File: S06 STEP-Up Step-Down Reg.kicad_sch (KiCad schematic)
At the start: 54 parts, among them Q16 IAUCN04S7L019, Q17 IAUCN04S7L028, Q18 CSD17304Q3, Q19 IAUCN04S7L019, U5 LM51772RHAR

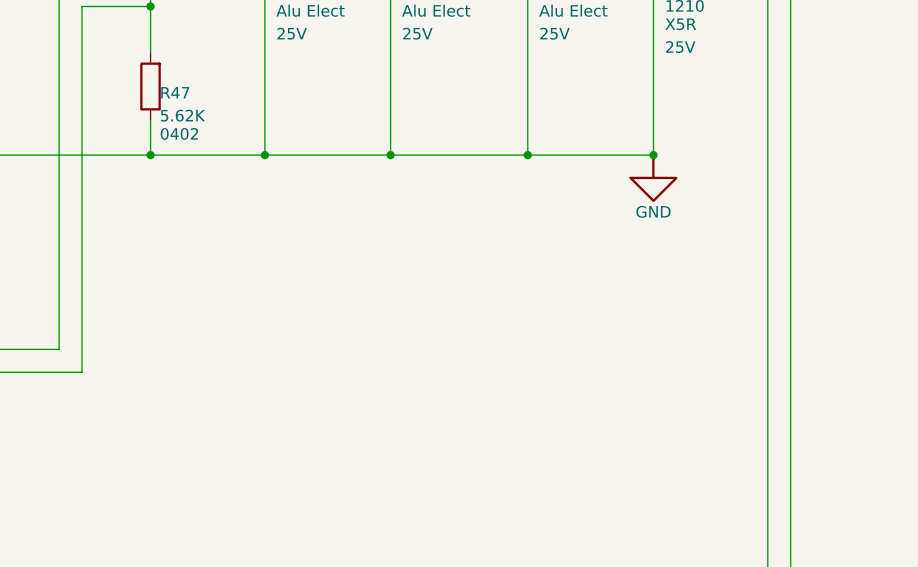
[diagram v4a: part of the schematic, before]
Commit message: Retune load-switch OVLO and PG dividers; add design constraint notes
- R90-R92 1M -> 1.07M: OVLO trips at 14.0 V (13.40-14.69 V) and recovers
  below 12.75 V (at least 12.23 V), so a tripped switch always comes back
  on the 12.03 V rail. R101 (Q23 gate divider) -> 1.07M to share the line.
- PGTH dividers R59/R61/R76 1M -> 100K and R60/R62/R77 130K -> 13K: same
  10.43 V threshold, but the +-1 uA pin leakage now moves it 0.1 V, not
  1 V; worst-case rising 10.93 V instead of 11.84 V.
- Schematic notes for the W16 constraints: J2 contacts (S01), R16 latching
  breaker and ED29/QE29 trip currents (S03), R19 vs L1 saturation (S04),
  R22 presence pull-up (S05), R42 and the U5 MODE/ILIMCOMP/VCC2 pins (S06),
  and the OVLO/PG divider settings (S07).
- README: OVLO and PG divider figures, and the EN_CONST_TDEAD default for
  the I2C build.

Co-Authored-By: Claude Opus 5.5 <noreply@anthropic.com>
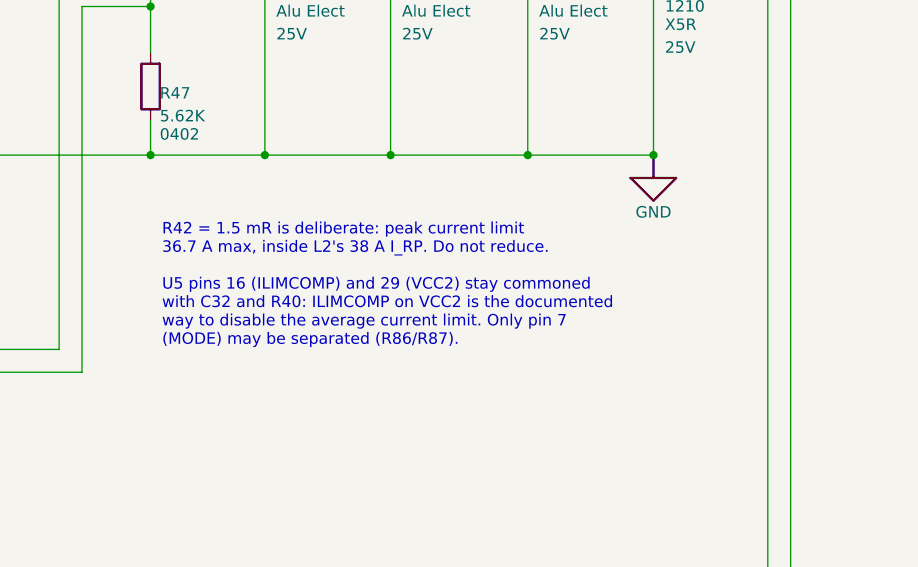
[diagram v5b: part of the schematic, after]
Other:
- note added: "R42 = 1.5 mR is deliberate: peak current limit 36.7 A max, inside L2's 38 A I_RP. Do not reduce. U5 pins 16 (ILIMCOMP) and 29 (VCC2) stay commoned with C32 and R40: ILIMCOMP on VCC2 is the documented way to disable the average current limit. Only pin 7 (MODE) may be separated (R86/R87)."
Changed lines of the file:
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@@
 	(generator_version "10.0")
 	(paper "A3")
+	(text "R42 = 1.5 mR is deliberate: peak current limit\n36.7 A max, inside L2's 38 A I_RP. Do not reduce.\n\nU5 pins 16 (ILIMCOMP) and 29 (VCC2) stay commoned\nwith C32 and R40: ILIMCOMP on VCC2 is the documented\nway to disable the average current limit. Only pin 7\n(MODE) may be separated (R86/R87)."
+		(exclude_from_sim no)
+		(at 292.1 100.33 0)
+		(effects
+			(font
+				(size 1.27 1.27)
+			)
+			(justify left top)
+		)
+	)
 	(text "1"
 		(exclude_from_sim no)

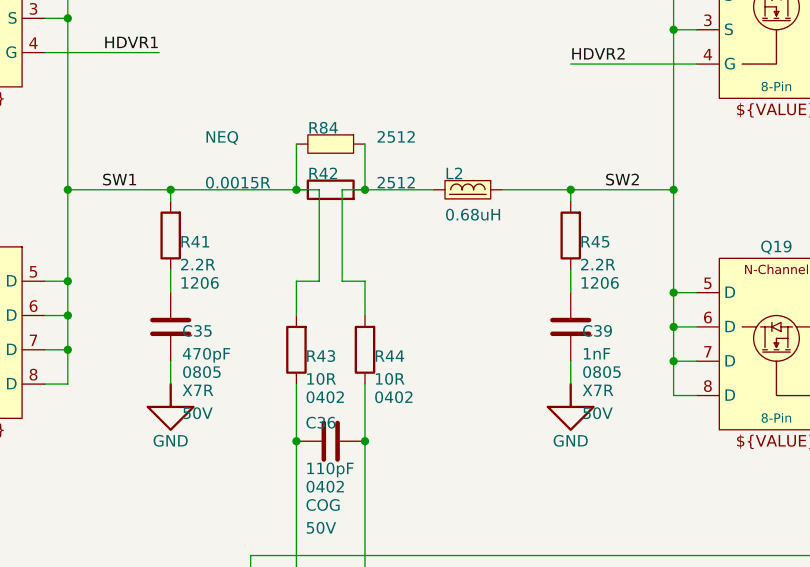
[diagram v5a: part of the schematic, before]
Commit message: Fit DMP3007SCG battery FETs and 1210 snubber resistors
- Q4, Q5, Q12-Q15: DMP3018SFV -> DMP3007SCG-13 (V-DFN3333-8 Type B) on
  KiCad's standard Package_SON:Diodes_PowerDI3333-8, which matches Diodes'
  Type B suggested land apart from 0.1 mm more toe per pad row. The new
  project symbol keeps the old pin positions and numbers D pins 5-8 and
  EP_D all 5, the footprint's single drain pad; all were already one net.
  The unused DMP3018SFV symbol is removed from the project library.
- R41, R45 (SW1/SW2 snubbers): 2.2R 1206 1/4 W -> 2.2R 1% 1210 1/2 W, any
  standard thick film. R41 runs at 75% (0.38 W worst case), R45 at 33%.
- README design-change rows for both.

The PCB still needs Update PCB from Schematic for these and the DAQ UVLO
parts.

Co-Authored-By: Claude Opus 5.5 <noreply@anthropic.com>
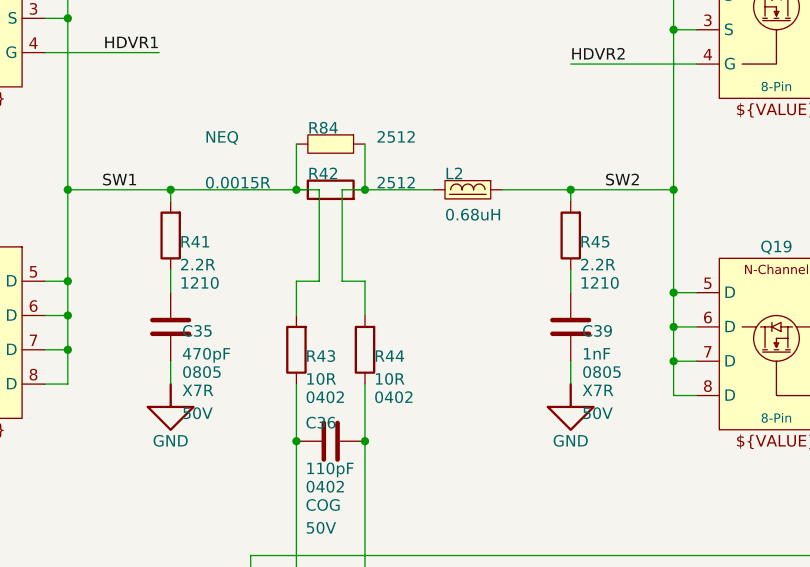
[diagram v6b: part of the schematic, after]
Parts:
- R41, R45: footprint Resistor_SMD:R_1206_3216Metric -> Resistor_SMD:R_1210_3225Metric; ALTIUM_FOOTPRINT 1206 -> 1210
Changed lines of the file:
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@@
 			)
 		)
-		(property "Footprint" "Resistor_SMD:R_1206_3216Metric"
+		(property "Footprint" "Resistor_SMD:R_1210_3225Metric"
 			(at 182.88 78.74 90)
 			(hide yes)
@@
 			)
 		)
-		(property "Description" "Resistor 2.2R 1% 1206"
+		(property "Description" "Resistor 2.2R 1% 1/2W 1210"
 			(at 182.88 78.74 90)
 			(hide yes)
@@
 			)
 		)
-		(property "ALTIUM_FOOTPRINT" "1206"
+		(property "ALTIUM_FOOTPRINT" "1210"
 			(at 183.896 83.312 0)
 			(show_name no)
@@
 			)
 		)
-		(property "Footprint" "Resistor_SMD:R_1206_3216Metric"
+		(property "Footprint" "Resistor_SMD:R_1210_3225Metric"
 			(at 227.33 78.74 90)
 			(hide yes)
@@
 			)
 		)
-		(property "Description" "Resistor 2.2R 1% 1206"
+		(property "Description" "Resistor 2.2R 1% 1/2W 1210"
 			(at 227.33 78.74 90)
 			(hide yes)
@@
 			)
 		)
-		(property "ALTIUM_FOOTPRINT" "1206"
+		(property "ALTIUM_FOOTPRINT" "1210"
 			(at 228.346 83.312 0)
 			(show_name no)

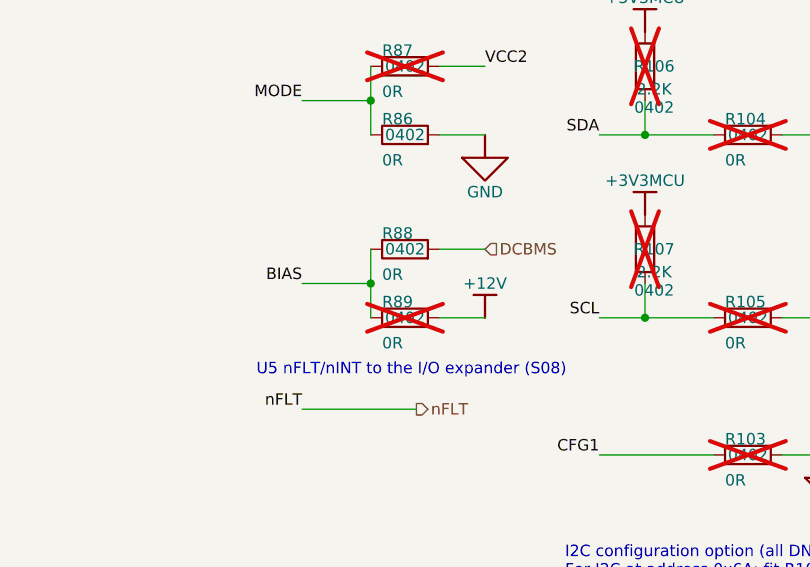
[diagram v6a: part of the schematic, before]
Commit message: Fit U5 BIAS to +12V by default; add firmware notes
- R89 fitted, R88 DNP: U5 BIAS on +12V, the LM51772 datasheet's standard
  configuration (§7.3.5). On the 24 V supply the VCC2 regulator drops from
  12 V instead of 24 V; VSMART falls back to VIN at start-up or if +12V
  collapses. nRST stays on DCBMS. The field units have BIAS on DCBMS.
- FIRMWARE_NOTES.md: SPI and expander set-up (inverted DAQ enable on P0_0,
  25% drive, polling, reset behaviour), load-switch thresholds, current
  monitor scaling, U5 I2C build defaults, LTC1960 breaker and R14 changes,
  and pack comms pass-through. Linked from the README.

Co-Authored-By: Claude Opus 5.5 <noreply@anthropic.com>
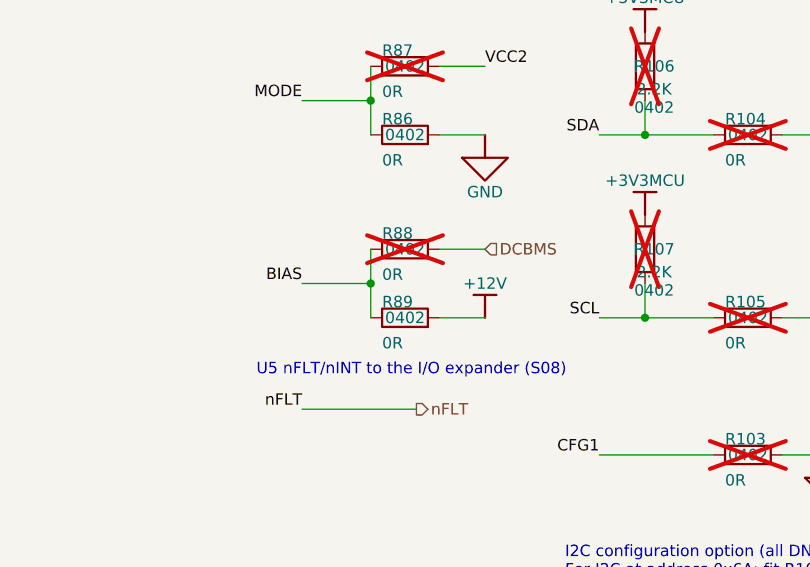
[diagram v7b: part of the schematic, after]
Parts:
- R88: now not fitted
- R89: now fitted
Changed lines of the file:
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@@
 		(on_board yes)
 		(in_pos_files yes)
-		(dnp no)
+		(dnp yes)
 		(property "Reference" "R88"
 			(at 280.67 209.804 90)
@@
 		(on_board yes)
 		(in_pos_files yes)
-		(dnp yes)
+		(dnp no)
 		(property "Reference" "R89"
 			(at 280.67 217.424 90)

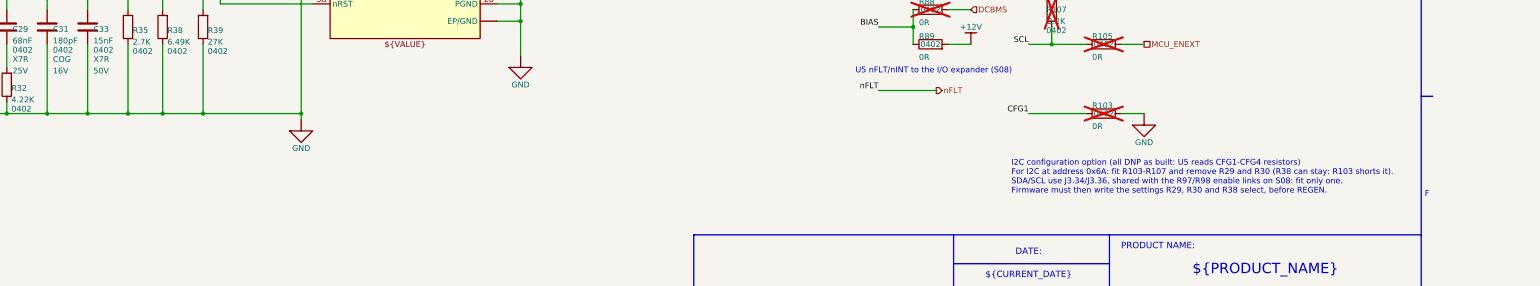
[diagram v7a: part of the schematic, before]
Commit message: Place the U5 option links; drop R103; PCB DRC clean-up
- Place the U5 MODE/BIAS links (R86-R89) and the CFG/I2C links near U5,
  clear of the +12V F.Cu pour.
- Move the I2C option links R104-R107 to a row beside J3 (between R12 and
  C56), next to J3.30 +3V3MCU, J3.34 and J3.36. GND F.Cu near J3 loses
  about 2 % with no new islands.
- Remove R103: the I2C build now changes R38 (CFG1) to 0R instead. Note
  added at R38 on S06; S06 I2C note, README and FIRMWARE_NOTES updated.
- Route the BIAS/MODE/VCC2 links and fix the DRC clearance, short and
  courtyard errors (manual edits in KiCad).

DRC with schematic parity: 285 violations, none clearance, short or
courtyard (library, padstack, silk and 63 unrouted pads remain).

Co-Authored-By: Claude Opus 5.5 <noreply@anthropic.com>
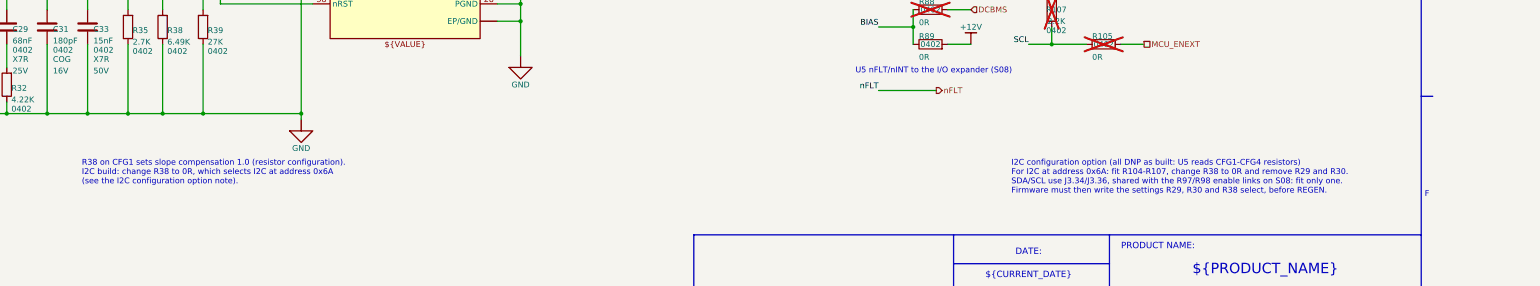
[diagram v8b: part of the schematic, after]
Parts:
- removed R103: 0R, Resistor_SMD:R_0402_1005Metric, symbol Device:R
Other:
- note added: "I2C configuration option (all DNP as built: U5 reads CFG1-CFG4 resistors) For I2C at address 0x6A: fit R104-R107, change R38 to 0R and remove R29 and R30. SDA/SCL use J3.34/J3.36, shared with the R97/R98 enable links on S08: fit only one. Firmware must then write the settings R29, R30 and R38 select, before REGEN."
- note added: "R38 on CFG1 sets slope compensation 1.0 (resistor configuration). I2C build: change R38 to 0R, which selects I2C at address 0x6A (see the I2C configuration option note)."
- note removed: "I2C configuration option (all DNP as built: U5 reads CFG1-CFG4 resistors) For I2C at address 0x6A: fit R103-R107 and remove R29 and R30 (R38 can stay: R103 shorts it). SDA/SCL use J3.34/J3.36, shared with the R97/R98 enable links on S08: fit only one. Firmware must then write the settings R29, R30 and R38 select, before REGEN."
